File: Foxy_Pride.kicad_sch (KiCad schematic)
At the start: 30 parts, among them U2 74HC4017D

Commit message: PCB layout editing
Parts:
- U1: value (none) -> TLC555CDR
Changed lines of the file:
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@@
       (effects (font (size 1.27 1.27)) (justify left))
     )
-    (property "Value" "" (id 1) (at 87.63 78.74 0)
+    (property "Value" "TLC555CDR" (id 1) (at 87.63 78.74 0)
       (effects (font (size 1.27 1.27)) (justify left))
     )

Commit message: PCB Layout
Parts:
- D1, D10, D2, D3, D4, D5, D6, D7, D8, D9: footprint Resistor_SMD:R_1206_3216Metric_Pad1.30x1.75mm_HandSolder -> Alpenglow:LED_1206+
- U1: footprint Package_SO:SOIC-8_3.9x4.9mm_P1.27mm -> Alpenglow:SO-8
- U2: footprint Package_SO:SOIC-16_3.9x9.9mm_P1.27mm -> Alpenglow:SO-16
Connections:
- net CLOCK: now reaches U1.3 (Q), U2.14 (CP0)
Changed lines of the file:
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@@
     (effects (font (size 2 2) italic) (justify left bottom))
+  )
+  (label "CLOCK" (at 111.76 68.58 0)
+    (effects (font (size 1.27 1.27)) (justify left bottom))
   )
   (symbol (lib_id "Alpenglow:CAP") (at 81.28 86.36 0) (unit 1)
@@
     (property "Reference" "D4" (id 0) (at 193.04 74.93 0))
     (property "Value" "LED" (id 1) (at 201.93 74.93 0))
-    (property "Footprint" "Resistor_SMD:R_1206_3216Metric_Pad1.30x1.75mm_HandSolder" (id 2) (at 196.85 76.2 90)
+    (property "Footprint" "Alpenglow:LED_1206+" (id 2) (at 196.85 76.2 90)
       (effects (font (size 1.27 1.27)) hide)
     )
@@
     (property "Reference" "D5" (id 0) (at 193.04 77.47 0))
     (property "Value" "LED" (id 1) (at 201.93 77.47 0))
-    (property "Footprint" "Resistor_SMD:R_1206_3216Metric_Pad1.30x1.75mm_HandSolder" (id 2) (at 196.85 78.74 90)
+    (property "Footprint" "Alpenglow:LED_1206+" (id 2) (at 196.85 78.74 90)
       (effects (font (size 1.27 1.27)) hide)
     )
@@
     (property "Reference" "D7" (id 0) (at 193.04 82.55 0))
     (property "Value" "LED" (id 1) (at 201.93 82.55 0))
-    (property "Footprint" "Resistor_SMD:R_1206_3216Metric_Pad1.30x1.75mm_HandSolder" (id 2) (at 196.85 83.82 90)
+    (property "Footprint" "Alpenglow:LED_1206+" (id 2) (at 196.85 83.82 90)
       (effects (font (size 1.27 1.27)) hide)
     )
@@
       (effects (font (size 1.27 1.27)) (justify left))
     )
-    (property "Footprint" "Package_SO:SOIC-8_3.9x4.9mm_P1.27mm" (id 2) (at 109.22 81.28 0)
+    (property "Footprint" "Alpenglow:SO-8" (id 2) (at 109.22 81.28 0)
       (effects (font (size 1.27 1.27)) hide)
     )
@@
     (property "Reference" "D9" (id 0) (at 193.04 87.63 0))
     (property "Value" "LED" (id 1) (at 201.93 87.63 0))
-    (property "Footprint" "Resistor_SMD:R_1206_3216Metric_Pad1.30x1.75mm_HandSolder" (id 2) (at 196.85 88.9 90)
+    (property "Footprint" "Alpenglow:LED_1206+" (id 2) (at 196.85 88.9 90)
       (effects (font (size 1.27 1.27)) hide)
     )
@@
     (property "Reference" "D1" (id 0) (at 193.04 67.31 0))
     (property "Value" "LED" (id 1) (at 201.93 67.31 0))
-    (property "Footprint" "Resistor_SMD:R_1206_3216Metric_Pad1.30x1.75mm_HandSolder" (id 2) (at 196.85 68.58 90)
+    (property "Footprint" "Alpenglow:LED_1206+" (id 2) (at 196.85 68.58 90)
       (effects (font (size 1.27 1.27)) hide)
     )
@@
     (property "Reference" "D10" (id 0) (at 193.04 90.17 0))
     (property "Value" "LED" (id 1) (at 201.93 90.17 0))
-    (property "Footprint" "Resistor_SMD:R_1206_3216Metric_Pad1.30x1.75mm_HandSolder" (id 2) (at 196.85 91.44 90)
+    (property "Footprint" "Alpenglow:LED_1206+" (id 2) (at 196.85 91.44 90)
       (effects (font (size 1.27 1.27)) hide)
     )
@@
     (property "Reference" "D2" (id 0) (at 193.04 69.85 0))
     (property "Value" "LED" (id 1) (at 201.93 69.85 0))
-    (property "Footprint" "Resistor_SMD:R_1206_3216Metric_Pad1.30x1.75mm_HandSolder" (id 2) (at 196.85 71.12 90)
+    (property "Footprint" "Alpenglow:LED_1206+" (id 2) (at 196.85 71.12 90)
       (effects (font (size 1.27 1.27)) hide)
     )
@@
     (property "Reference" "D3" (id 0) (at 193.04 72.39 0))
     (property "Value" "LED" (id 1) (at 201.93 72.39 0))
-    (property "Footprint" "Resistor_SMD:R_1206_3216Metric_Pad1.30x1.75mm_HandSolder" (id 2) (at 196.85 73.66 90)
+    (property "Footprint" "Alpenglow:LED_1206+" (id 2) (at 196.85 73.66 90)
       (effects (font (size 1.27 1.27)) hide)
     )
@@
     (property "Reference" "D8" (id 0) (at 193.04 85.09 0))
     (property "Value" "LED" (id 1) (at 201.93 85.09 0))
-    (property "Footprint" "Resistor_SMD:R_1206_3216Metric_Pad1.30x1.75mm_HandSolder" (id 2) (at 196.85 86.36 90)
+    (property "Footprint" "Alpenglow:LED_1206+" (id 2) (at 196.85 86.36 90)
       (effects (font (size 1.27 1.27)) hide)
     )
@@
     (property "Reference" "U2" (id 0) (at 162.56 66.04 0))
     (property "Value" "74HC4017D" (id 1) (at 167.64 99.06 0))
-    (property "Footprint" "Package_SO:SOIC-16_3.9x9.9mm_P1.27mm" (id 2) (at 157.48 82.55 0)
+    (property "Footprint" "Alpenglow:SO-16" (id 2) (at 157.48 82.55 0)
       (effects (font (size 1.27 1.27)) hide)
     )
@@
     (property "Reference" "D6" (id 0) (at 193.04 80.01 0))
     (property "Value" "LED" (id 1) (at 201.93 80.01 0))
-    (property "Footprint" "Resistor_SMD:R_1206_3216Metric_Pad1.30x1.75mm_HandSolder" (id 2) (at 196.85 81.28 90)
+    (property "Footprint" "Alpenglow:LED_1206+" (id 2) (at 196.85 81.28 90)
       (effects (font (size 1.27 1.27)) hide)
     )
@@
     )
     (path "/6106dfe1-f48b-4398-a5ac-71221fc276a2"
-      (reference "D1") (unit 1) (value "LED") (footprint "Resistor_SMD:R_1206_3216Metric_Pad1.30x1.75mm_HandSolder")
+      (reference "D1") (unit 1) (value "LED") (footprint "Alpenglow:LED_1206+")
     )
     (path "/6f24fd24-8691-4653-ad89-566c30b8ec8b"
-      (reference "D2") (unit 1) (value "LED") (footprint "Resistor_SMD:R_1206_3216Metric_Pad1.30x1.75mm_HandSolder")
+      (reference "D2") (unit 1) (value "LED") (footprint "Alpenglow:LED_1206+")
     )
     (path "/6f64d9a0-48ae-4cf9-a701-dc36ec0b4ac9"
-      (reference "D3") (unit 1) (value "LED") (footprint "Resistor_SMD:R_1206_3216Metric_Pad1.30x1.75mm_HandSolder")
+      (reference "D3") (unit 1) (value "LED") (footprint "Alpenglow:LED_1206+")
     )
     (path "/1bde712a-3a34-49c0-a4c6-f4b541033fbb"
-      (reference "D4") (unit 1) (value "LED") (footprint "Resistor_SMD:R_1206_3216Metric_Pad1.30x1.75mm_HandSolder")
+      (reference "D4") (unit 1) (value "LED") (footprint "Alpenglow:LED_1206+")
     )
     (path "/2905a1eb-53c3-456c-b719-8f57fd351add"
-      (reference "D5") (unit 1) (value "LED") (footprint "Resistor_SMD:R_1206_3216Metric_Pad1.30x1.75mm_HandSolder")
+      (reference "D5") (unit 1) (value "LED") (footprint "Alpenglow:LED_1206+")
     )
     (path "/e3c4d955-1366-45fb-9e2b-c0fbcee1729f"
-      (reference "D6") (unit 1) (value "LED") (footprint "Resistor_SMD:R_1206_3216Metric_Pad1.30x1.75mm_HandSolder")
+      (reference "D6") (unit 1) (value "LED") (footprint "Alpenglow:LED_1206+")
     )
     (path "/2a33de0e-cd42-4d90-a52a-8f22807b5895"
-      (reference "D7") (unit 1) (value "LED") (footprint "Resistor_SMD:R_1206_3216Metric_Pad1.30x1.75mm_HandSolder")
+      (reference "D7") (unit 1) (value "LED") (footprint "Alpenglow:LED_1206+")
     )
     (path "/b2e0f1e6-e565-4f86-8b0b-7e6dc09e9fe2"
-      (reference "D8") (unit 1) (value "LED") (footprint "Resistor_SMD:R_1206_3216Metric_Pad1.30x1.75mm_HandSolder")
+      (reference "D8") (unit 1) (value "LED") (footprint "Alpenglow:LED_1206+")
     )
     (path "/3c85f448-4ac8-4bce-95ee-3b8f8de4fbd0"
-      (reference "D9") (unit 1) (value "LED") (footprint "Resistor_SMD:R_1206_3216Metric_Pad1.30x1.75mm_HandSolder")
+      (reference "D9") (unit 1) (value "LED") (footprint "Alpenglow:LED_1206+")
     )
     (path "/68c9c88a-ccc8-46b9-a142-182570d21f72"
-      (reference "D10") (unit 1) (value "LED") (footprint "Resistor_SMD:R_1206_3216Metric_Pad1.30x1.75mm_HandSolder")
+      (reference "D10") (unit 1) (value "LED") (footprint "Alpenglow:LED_1206+")
     )
     (path "/1b4201e5-9ece-48ea-b3c7-c70ad9466a1d"
@@
     )
     (path "/3640318e-2da3-4d2b-8912-c4c45acaae63"
-      (reference "U1") (unit 1) (value "TLC555CDR") (footprint "Package_SO:SOIC-8_3.9x4.9mm_P1.27mm")
+      (reference "U1") (unit 1) (value "TLC555CDR") (footprint "Alpenglow:SO-8")
     )
     (path "/d05e5bb8-2fc4-4d16-87a5-4e0682effe41"
-      (reference "U2") (unit 1) (value "74HC4017D") (footprint "Package_SO:SOIC-16_3.9x9.9mm_P1.27mm")
-    )
-  )
+      (reference "U2") (unit 1) (value "74HC4017D") (footprint "Alpenglow:SO-16")
+    )
+  )

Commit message: Finalized design and layout on Foxy Pride PCB
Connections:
- net +Vbatt: now reaches BT1.1 (+), S1.1
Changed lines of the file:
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@@
   (junction (at 205.74 78.74) (diameter 0) (color 0 0 0 0)
+  )
+  (junction (at 30.48 29.21) (diameter 0) (color 0 0 0 0)
   )
   (junction (at 81.28 49.53) (diameter 0) (color 0 0 0 0)
@@
     (stroke (width 0) (type default) (color 0 0 0 0))
   )
+  (wire (pts (xy 30.48 29.21) (xy 26.67 29.21))
+    (stroke (width 0) (type default) (color 0 0 0 0))
+  )
   (wire (pts (xy 81.28 49.53) (xy 81.28 55.88))
     (stroke (width 0) (type default) (color 0 0 0 0))
@@
     (stroke (width 0) (type default) (color 0 0 0 0))
   )
-  (wire (pts (xy 34.29 29.21) (xy 26.67 29.21))
+  (wire (pts (xy 34.29 29.21) (xy 30.48 29.21))
     (stroke (width 0) (type default) (color 0 0 0 0))
   )
@@
     (pin "1")
     (pin "2")
+  )
+  (symbol (lib_id "Alpenglow:+Vbatt") (at 25.4 29.21 0) (unit 1)
+    (in_bom yes) (on_board yes) (fields_autoplaced)
+    (property "Reference" "#PWR0101" (id 0) (at 25.4 33.02 0)
+      (effects (font (size 1.27 1.27)) hide)
+    )
+    (property "Value" "+Vbatt" (id 1) (at 30.48 25.4785 0))
+    (property "Footprint" "" (id 2) (at 25.4 29.21 0)
+      (effects (font (size 1.27 1.27)) hide)
+    )
+    (property "Datasheet" "" (id 3) (at 25.4 29.21 0)
+      (effects (font (size 1.27 1.27)) hide)
+    )
+    (pin "")
   )
   (symbol (lib_id "Device:Battery_Cell") (at 26.67 38.1 0) (unit 1)
@@
       (reference "#PWR010") (unit 1) (value "GND") (footprint "")
     )
+    (path "/0f81970b-f55e-4039-a8ff-40c0a07bab88"
+      (reference "#PWR0101") (unit 1) (value "+Vbatt") (footprint "")
+    )
     (path "/131ab8e4-c54e-4e61-8d99-1adb96275252"

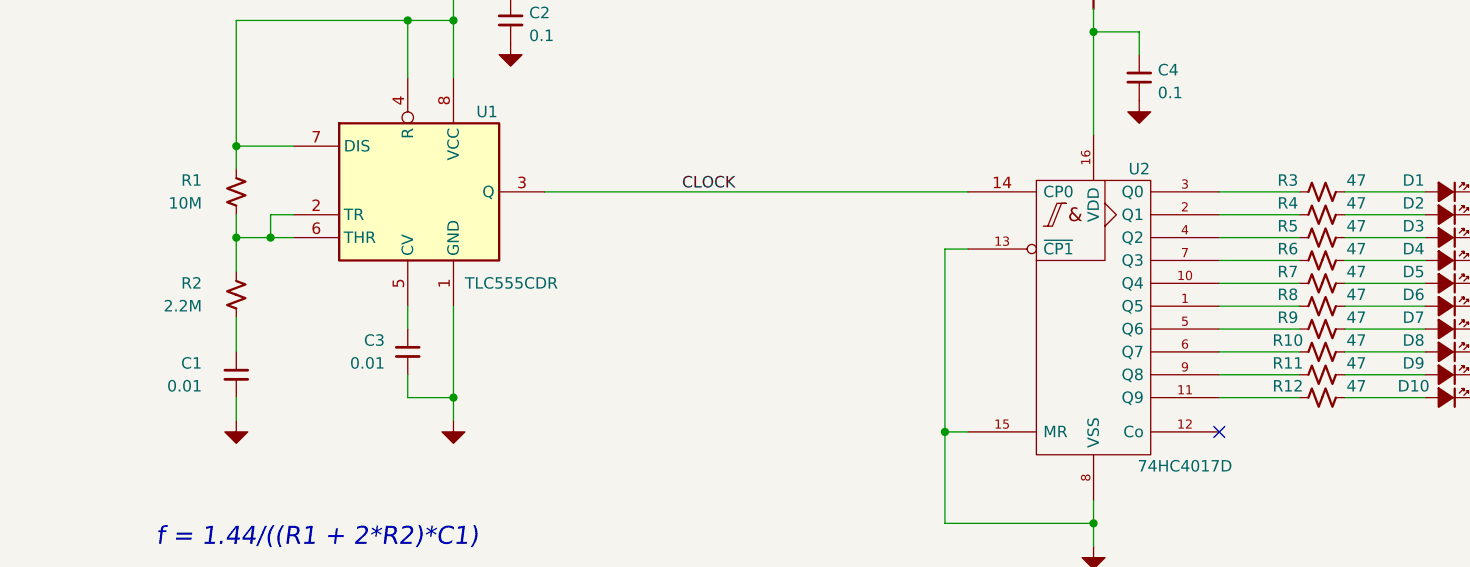
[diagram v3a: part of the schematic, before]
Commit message: Re annontated schematic so resistors and LEDs have matching refrence designators
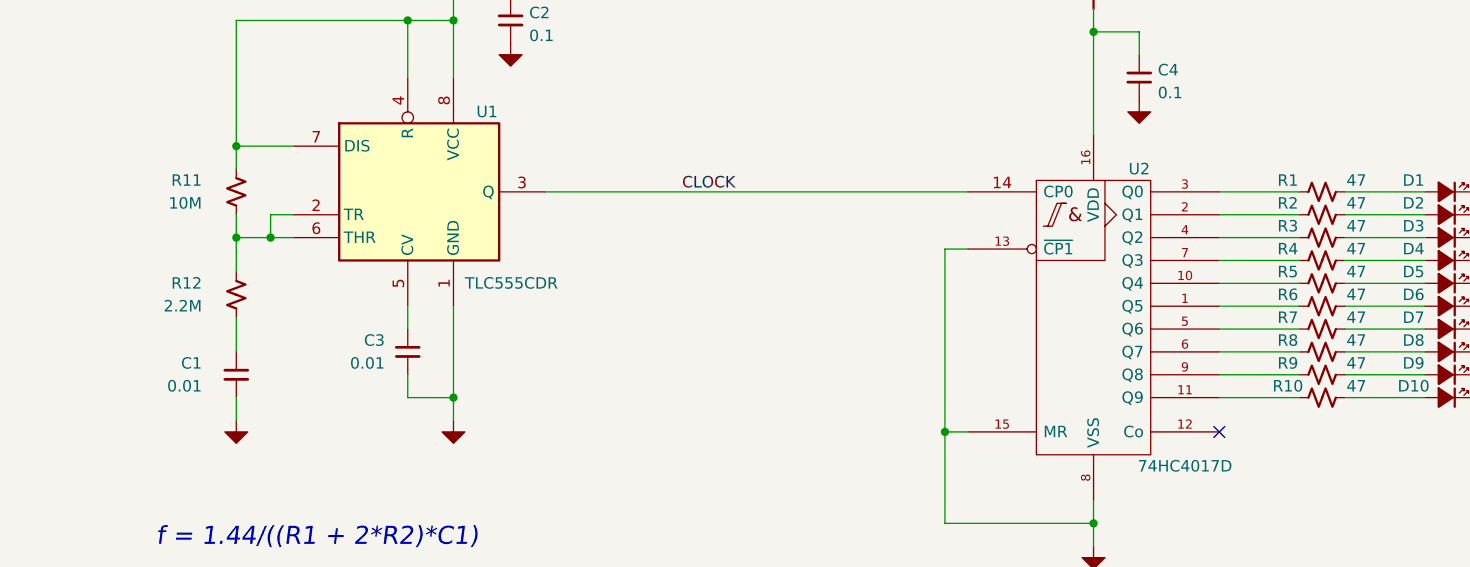
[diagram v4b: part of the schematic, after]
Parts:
- renumbered R3 to R1, R12 to R10, R1 to R11, R2 to R12, R4 to R2, R5 to R3, R6 to R4, R7 to R5, R8 to R6, R9 to R7, R10 to R8, R11 to R9
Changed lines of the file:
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@@
   (symbol (lib_id "Alpenglow:RES") (at 62.23 68.58 0) (unit 1)
     (in_bom yes) (on_board yes)
-    (property "Reference" "R1" (id 0) (at 58.42 67.31 0)
+    (property "Reference" "R11" (id 0) (at 58.42 67.31 0)
       (effects (font (size 1.27 1.27)) (justify right))
     )
@@
   (symbol (lib_id "Alpenglow:RES") (at 182.88 78.74 270) (unit 1)
     (in_bom yes) (on_board yes)
-    (property "Reference" "R7" (id 0) (at 179.07 77.47 90))
+    (property "Reference" "R5" (id 0) (at 179.07 77.47 90))
     (property "Value" "47" (id 1) (at 186.69 77.47 90))
     (property "Footprint" "Resistor_SMD:R_1206_3216Metric_Pad1.30x1.75mm_HandSolder" (id 2) (at 182.88 78.74 0)
@@
   (symbol (lib_id "Alpenglow:RES") (at 182.88 83.82 270) (unit 1)
     (in_bom yes) (on_board yes)
-    (property "Reference" "R9" (id 0) (at 179.07 82.55 90))
+    (property "Reference" "R7" (id 0) (at 179.07 82.55 90))
     (property "Value" "47" (id 1) (at 186.69 82.55 90))
     (property "Footprint" "Resistor_SMD:R_1206_3216Metric_Pad1.30x1.75mm_HandSolder" (id 2) (at 182.88 83.82 0)
@@
   (symbol (lib_id "Alpenglow:RES") (at 182.88 81.28 270) (unit 1)
     (in_bom yes) (on_board yes)
-    (property "Reference" "R8" (id 0) (at 179.07 80.01 90))
+    (property "Reference" "R6" (id 0) (at 179.07 80.01 90))
     (property "Value" "47" (id 1) (at 186.69 80.01 90))
     (property "Footprint" "Resistor_SMD:R_1206_3216Metric_Pad1.30x1.75mm_HandSolder" (id 2) (at 182.88 81.28 0)
@@
   (symbol (lib_id "Alpenglow:RES") (at 182.88 71.12 270) (unit 1)
     (in_bom yes) (on_board yes)
-    (property "Reference" "R4" (id 0) (at 179.07 69.85 90))
+    (property "Reference" "R2" (id 0) (at 179.07 69.85 90))
     (property "Value" "47" (id 1) (at 186.69 69.85 90))
     (property "Footprint" "Resistor_SMD:R_1206_3216Metric_Pad1.30x1.75mm_HandSolder" (id 2) (at 182.88 71.12 0)
@@
   (symbol (lib_id "Alpenglow:RES") (at 62.23 80.01 0) (unit 1)
     (in_bom yes) (on_board yes)
-    (property "Reference" "R2" (id 0) (at 58.42 78.74 0)
+    (property "Reference" "R12" (id 0) (at 58.42 78.74 0)
       (effects (font (size 1.27 1.27)) (justify right))
     )
@@
   (symbol (lib_id "Alpenglow:RES") (at 182.88 68.58 270) (unit 1)
     (in_bom yes) (on_board yes)
-    (property "Reference" "R3" (id 0) (at 179.07 67.31 90))
+    (property "Reference" "R1" (id 0) (at 179.07 67.31 90))
     (property "Value" "47" (id 1) (at 186.69 67.31 90))
     (property "Footprint" "Resistor_SMD:R_1206_3216Metric_Pad1.30x1.75mm_HandSolder" (id 2) (at 182.88 68.58 0)
@@
   (symbol (lib_id "Alpenglow:RES") (at 182.88 86.36 270) (unit 1)
     (in_bom yes) (on_board yes)
-    (property "Reference" "R10" (id 0) (at 179.07 85.09 90))
+    (property "Reference" "R8" (id 0) (at 179.07 85.09 90))
     (property "Value" "47" (id 1) (at 186.69 85.09 90))
     (property "Footprint" "Resistor_SMD:R_1206_3216Metric_Pad1.30x1.75mm_HandSolder" (id 2) (at 182.88 86.36 0)
@@
   (symbol (lib_id "Alpenglow:RES") (at 182.88 88.9 270) (unit 1)
     (in_bom yes) (on_board yes)
-    (property "Reference" "R11" (id 0) (at 179.07 87.63 90))
+    (property "Reference" "R9" (id 0) (at 179.07 87.63 90))
     (property "Value" "47" (id 1) (at 186.69 87.63 90))
     (property "Footprint" "Resistor_SMD:R_1206_3216Metric_Pad1.30x1.75mm_HandSolder" (id 2) (at 182.88 88.9 0)
@@
   (symbol (lib_id "Alpenglow:RES") (at 182.88 91.44 270) (unit 1)
     (in_bom yes) (on_board yes)
-    (property "Reference" "R12" (id 0) (at 179.07 90.17 90))
+    (property "Reference" "R10" (id 0) (at 179.07 90.17 90))
     (property "Value" "47" (id 1) (at 186.69 90.17 90))
     (property "Footprint" "Resistor_SMD:R_1206_3216Metric_Pad1.30x1.75mm_HandSolder" (id 2) (at 182.88 91.44 0)
@@
   (symbol (lib_id "Alpenglow:RES") (at 182.88 76.2 270) (unit 1)
     (in_bom yes) (on_board yes)
-    (property "Reference" "R6" (id 0) (at 179.07 74.93 90))
+    (property "Reference" "R4" (id 0) (at 179.07 74.93 90))
     (property "Value" "47" (id 1) (at 186.69 74.93 90))
     (property "Footprint" "Resistor_SMD:R_1206_3216Metric_Pad1.30x1.75mm_HandSolder" (id 2) (at 182.88 76.2 0)
@@
   (symbol (lib_id "Alpenglow:RES") (at 182.88 73.66 270) (unit 1)
     (in_bom yes) (on_board yes)
-    (property "Reference" "R5" (id 0) (at 179.07 72.39 90))
+    (property "Reference" "R3" (id 0) (at 179.07 72.39 90))
     (property "Value" "47" (id 1) (at 186.69 72.39 90))
     (property "Footprint" "Resistor_SMD:R_1206_3216Metric_Pad1.30x1.75mm_HandSolder" (id 2) (at 182.88 73.66 0)
@@
       (reference "D10") (unit 1) (value "LED") (footprint "Alpenglow:LED_1206+")
     )
+    (path "/8c6438e0-c7f7-4855-af64-fea1be0fb344"
+      (reference "R1") (unit 1) (value "47") (footprint "Resistor_SMD:R_1206_3216Metric_Pad1.30x1.75mm_HandSolder")
+    )
+    (path "/6ad65c37-7515-4fb3-aaf8-1a0633093c90"
+      (reference "R2") (unit 1) (value "47") (footprint "Resistor_SMD:R_1206_3216Metric_Pad1.30x1.75mm_HandSolder")
+    )
+    (path "/ff370708-eb70-465c-b329-5b91dba784e7"
+      (reference "R3") (unit 1) (value "47") (footprint "Resistor_SMD:R_1206_3216Metric_Pad1.30x1.75mm_HandSolder")
+    )
+    (path "/fba92b72-9c35-4809-b005-9566acf3bb56"
+      (reference "R4") (unit 1) (value "47") (footprint "Resistor_SMD:R_1206_3216Metric_Pad1.30x1.75mm_HandSolder")
+    )
+    (path "/415b5bcb-ce3a-4ae4-88b8-e0302aed570d"
+      (reference "R5") (unit 1) (value "47") (footprint "Resistor_SMD:R_1206_3216Metric_Pad1.30x1.75mm_HandSolder")
+    )
+    (path "/5b4cf8d6-c0a2-41e0-afe5-487bdbeb6172"
+      (reference "R6") (unit 1) (value "47") (footprint "Resistor_SMD:R_1206_3216Metric_Pad1.30x1.75mm_HandSolder")
+    )
+    (path "/4fcc2f77-0c5c-4b07-a8e6-5ce162179cf6"
+      (reference "R7") (unit 1) (value "47") (footprint "Resistor_SMD:R_1206_3216Metric_Pad1.30x1.75mm_HandSolder")
+    )
+    (path "/9993ec78-1894-4929-824d-5c3bfb26c5ed"
+      (reference "R8") (unit 1) (value "47") (footprint "Resistor_SMD:R_1206_3216Metric_Pad1.30x1.75mm_HandSolder")
+    )
+    (path "/c1f6c31b-816f-4257-b340-64f3f18e6208"
+      (reference "R9") (unit 1) (value "47") (footprint "Resistor_SMD:R_1206_3216Metric_Pad1.30x1.75mm_HandSolder")
+    )
+    (path "/ee03b992-583c-45bd-8457-e2bf46e95793"
+      (reference "R10") (unit 1) (value "47") (footprint "Resistor_SMD:R_1206_3216Metric_Pad1.30x1.75mm_HandSolder")
+    )
     (path "/1b4201e5-9ece-48ea-b3c7-c70ad9466a1d"
-      (reference "R1") (unit 1) (value "10M") (footprint "Resistor_SMD:R_1206_3216Metric_Pad1.30x1.75mm_HandSolder")
+      (reference "R11") (unit 1) (value "10M") (footprint "Resistor_SMD:R_1206_3216Metric_Pad1.30x1.75mm_HandSolder")
     )
     (path "/7008e248-661c-4c7c-b274-d987c71690ff"
-      (reference "R2") (unit 1) (value "2.2M") (footprint "Resistor_SMD:R_1206_3216Metric_Pad1.30x1.75mm_HandSolder")
-    )
-    (path "/8c6438e0-c7f7-4855-af64-fea1be0fb344"
-      (reference "R3") (unit 1) (value "47") (footprint "Resistor_SMD:R_1206_3216Metric_Pad1.30x1.75mm_HandSolder")
-    )
-    (path "/6ad65c37-7515-4fb3-aaf8-1a0633093c90"
-      (reference "R4") (unit 1) (value "47") (footprint "Resistor_SMD:R_1206_3216Metric_Pad1.30x1.75mm_HandSolder")
-    )
-    (path "/ff370708-eb70-465c-b329-5b91dba784e7"
-      (reference "R5") (unit 1) (value "47") (footprint "Resistor_SMD:R_1206_3216Metric_Pad1.30x1.75mm_HandSolder")
-    )
-    (path "/fba92b72-9c35-4809-b005-9566acf3bb56"
-      (reference "R6") (unit 1) (value "47") (footprint "Resistor_SMD:R_1206_3216Metric_Pad1.30x1.75mm_HandSolder")
-    )
-    (path "/415b5bcb-ce3a-4ae4-88b8-e0302aed570d"
-      (reference "R7") (unit 1) (value "47") (footprint "Resistor_SMD:R_1206_3216Metric_Pad1.30x1.75mm_HandSolder")
-    )
-    (path "/5b4cf8d6-c0a2-41e0-afe5-487bdbeb6172"
-      (reference "R8") (unit 1) (value "47") (footprint "Resistor_SMD:R_1206_3216Metric_Pad1.30x1.75mm_HandSolder")
-    )
-    (path "/4fcc2f77-0c5c-4b07-a8e6-5ce162179cf6"
-      (reference "R9") (unit 1) (value "47") (footprint "Resistor_SMD:R_1206_3216Metric_Pad1.30x1.75mm_HandSolder")
-    )
-    (path "/9993ec78-1894-4929-824d-5c3bfb26c5ed"
-      (reference "R10") (unit 1) (value "47") (footprint "Resistor_SMD:R_1206_3216Metric_Pad1.30x1.75mm_HandSolder")
-    )
-    (path "/c1f6c31b-816f-4257-b340-64f3f18e6208"
-      (reference "R11") (unit 1) (value "47") (footprint "Resistor_SMD:R_1206_3216Metric_Pad1.30x1.75mm_HandSolder")
-    )
-    (path "/ee03b992-583c-45bd-8457-e2bf46e95793"
-      (reference "R12") (unit 1) (value "47") (footprint "Resistor_SMD:R_1206_3216Metric_Pad1.30x1.75mm_HandSolder")
+      (reference "R12") (unit 1) (value "2.2M") (footprint "Resistor_SMD:R_1206_3216Metric_Pad1.30x1.75mm_HandSolder")
     )
     (path "/c88ff2f0-5b88-46b4-ac97-70401271d31a"
